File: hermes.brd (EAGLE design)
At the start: 22.9 x 35.1 mm, 36 parts

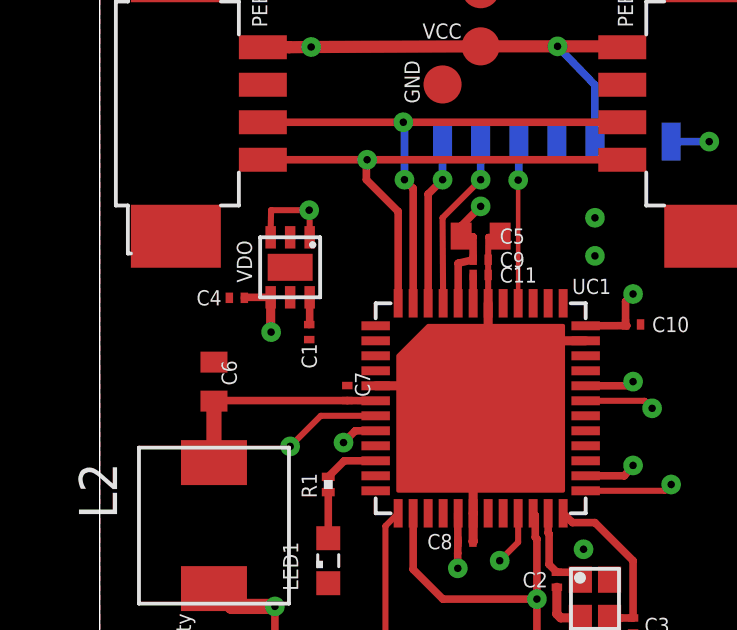
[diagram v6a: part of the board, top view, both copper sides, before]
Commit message: -Update component description in library -Generate new BOM and CAM files from new configuration -Delete outdated layout and cam documents
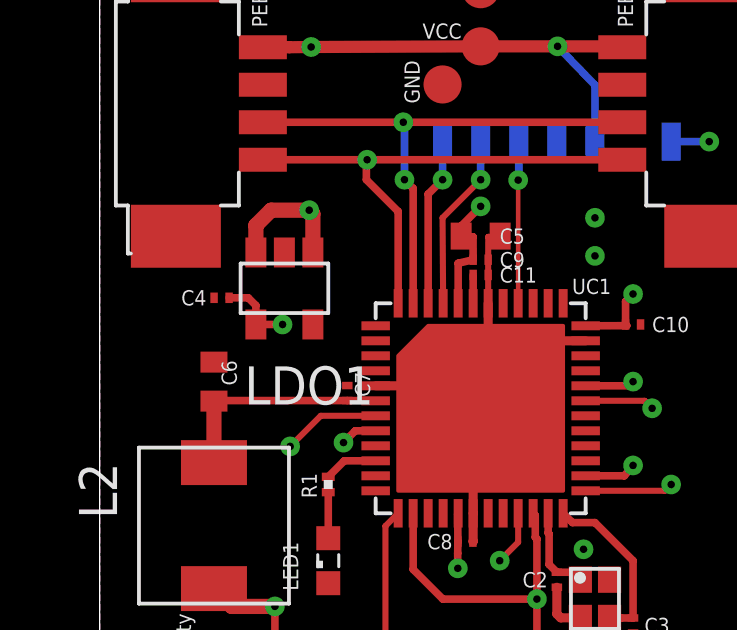
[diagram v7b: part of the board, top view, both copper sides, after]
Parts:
- removed C1: 470pF, rcl:C0201
- removed VDO: MIC5219-3.3BML, Hermes_lib:MLF-6
- added LDO1: MIC5231-3.3BM5, Hermes_lib:SOT-23-5
- moved C4 0.51 mm to (40.9, 32.9)
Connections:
- removed net N$2: C1.1, VDO.P$6
- net +3V3: now also LDO1.P$4; no longer VDO.P$4
- net GND: now also LDO1.P$2; no longer C1.2, VDO.P$2, VDO.P$7
- net VCC: now also LDO1.P$1, LDO1.P$3; no longer VDO.P$1, VDO.P$3
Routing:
- net VCC: track 24.2 -> 25.5 mm
- net N$2: track 0.92 -> 0.00 mm
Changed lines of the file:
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@@
 </autorouter>
 <elements>
-<element name="C1" library="rcl" library_urn="urn:adsk.eagle:library:334" package="C0201" package3d_urn="urn:adsk.eagle:package:23690/1" value="470pF" x="43.815" y="31.75" smashed="yes" rot="R270">
-<attribute name="NAME" x="43.561" y="31.369" size="0.508" layer="25" rot="R270"/>
-<attribute name="VALUE" x="41.91" y="32.385" size="0.508" layer="27" rot="R270"/>
-</element>
 <element name="C10" library="rcl" library_urn="urn:adsk.eagle:library:334" package="C0201" package3d_urn="urn:adsk.eagle:package:23690/1" value="100nF" x="54.61" y="32.004" smashed="yes">
 <attribute name="NAME" x="55.245" y="31.75" size="0.508" layer="25"/>
@@
 <attribute name="VALUE" x="52.705" y="22.606" size="0.508" layer="27" rot="R270"/>
 </element>
-<element name="C4" library="rcl" library_urn="urn:adsk.eagle:library:334" package="C0201" package3d_urn="urn:adsk.eagle:package:23690/1" value="2.2uF" x="41.402" y="32.893" smashed="yes" rot="R180">
-<attribute name="NAME" x="40.894" y="33.147" size="0.508" layer="25" rot="R180"/>
-<attribute name="VALUE" x="42.037" y="34.798" size="0.508" layer="27" rot="R180"/>
+<element name="C4" library="rcl" library_urn="urn:adsk.eagle:library:334" package="C0201" package3d_urn="urn:adsk.eagle:package:23690/1" value="2.2uF" x="40.894" y="32.893" smashed="yes" rot="R180">
+<attribute name="NAME" x="40.386" y="33.147" size="0.508" layer="25" rot="R180"/>
+<attribute name="VALUE" x="41.529" y="34.798" size="0.508" layer="27" rot="R180"/>
 </element>
 <element name="C5" library="rcl" library_urn="urn:adsk.eagle:library:334" package="C0402" package3d_urn="urn:adsk.eagle:package:23626/1" value="10uF" x="49.53" y="34.9504" smashed="yes">
@@
 <element name="PEER2" library="Hermes_lib" package="PICO-BLADE4" value="PICO-BLADE4" x="57.15" y="39.37" smashed="yes" rot="R90">
 <attribute name="NAME" x="54.61" y="41.91" size="0.508" layer="25" rot="R90"/>
-</element>
-<element name="VDO" library="Hermes_lib" package="MLF-6" value="MIC5219-3.3BML" x="43.18" y="33.909" smashed="yes" rot="R270">
-<attribute name="NAME" x="41.91" y="33.401" size="0.508" layer="25" rot="R90"/>
-<attribute name="VALUE" x="41.68" y="34.909" size="0.508" layer="27" rot="R270"/>
 </element>
 <element name="LED1" library="eagle-ltspice" library_urn="urn:adsk.eagle:library:217" package="LED_SML0603" package3d_urn="urn:adsk.eagle:package:13315/1" value="" x="44.45" y="24.13" smashed="yes" rot="R90">
@@
 </element>
 <element name="L2" library="Hermes_lib" package="L2215" value="10uH" x="40.64" y="25.4" rot="R270"/>
+<element name="LDO1" library="Hermes_lib" package="SOT-23-5" value="MIC5231-3.3BM5" x="42.926" y="33.147"/>
 </elements>
 <signals>
@@
 <contactref element="UC1" pad="P$36"/>
 <contactref element="C8" pad="1"/>
-<contactref element="VDO" pad="P$4"/>
 <contactref element="C4" pad="1"/>
 <contactref element="R4" pad="1"/>
@@
 <contactref element="R5" pad="2"/>
 <contactref element="SLAVE" pad="P$9"/>
-<wire x1="41.668" y1="32.909" x2="42.53" y2="32.909" width="0.254" layer="1"/>
-<wire x1="41.668" y1="32.909" x2="41.652" y2="32.893" width="0.254" layer="1"/>
 <polygon width="0.3048" layer="2">
 <vertex x="36.83" y="46.355"/>
@@
 <vertex x="59.69" y="46.355"/>
 </polygon>
-<wire x1="42.53" y1="32.909" x2="42.53" y2="31.765" width="0.3048" layer="1"/>
-<wire x1="42.53" y1="31.765" x2="42.545" y2="31.75" width="0.3048" layer="1"/>
-<via x="42.545" y="31.75" extent="1-16" drill="0.25"/>
 <wire x1="52.655" y1="16.743" x2="52.655" y2="18.873" width="0.3048" layer="1"/>
 <wire x1="52.655" y1="18.873" x2="52.705" y2="18.923" width="0.3048" layer="1"/>
@@
 <wire x1="42.672" y1="22.606" x2="41.234" y2="22.606" width="0.508" layer="1"/>
 <wire x1="41.234" y1="22.606" x2="40.64" y2="23.2" width="0.508" layer="1"/>
+<contactref element="LDO1" pad="P$4"/>
+<via x="42.926" y="32.004" extent="1-16" drill="0.25"/>
+<wire x1="41.144" y1="32.893" x2="41.783" y2="32.893" width="0.254" layer="1"/>
+<wire x1="41.783" y1="32.893" x2="42.037" y2="32.639" width="0.254" layer="1"/>
+<wire x1="42.037" y1="32.639" x2="42.037" y2="32.004" width="0.254" layer="1"/>
+<wire x1="42.037" y1="32.004" x2="42.926" y2="32.004" width="0.254" layer="1"/>
 </signal>
 <signal name="GND">
@@
 <contactref element="C8" pad="2"/>
 <contactref element="C4" pad="2"/>
-<contactref element="VDO" pad="P$2"/>
 <contactref element="LED1" pad="C"/>
 <contactref element="LED2" pad="C"/>
 <contactref element="C2" pad="2"/>
 <contactref element="C3" pad="2"/>
-<contactref element="C1" pad="2"/>
 <contactref element="XTAL" pad="GND@2"/>
 <contactref element="XTAL" pad="GND@1"/>
@@
 <vertex x="59.69" y="46.355"/>
 </polygon>
-<contactref element="VDO" pad="P$7"/>
 <wire x1="49.28" y1="28.96" x2="49.28" y2="25.71" width="0.3048" layer="1"/>
 <wire x1="49.53" y1="29.21" x2="49.28" y2="28.96" width="0.3048" layer="1"/>
@@
 <vertex x="59.69" y="11.303"/>
 </polygon>
+<contactref element="LDO1" pad="P$2"/>
 </signal>
 <signal name="VCC">
-<contactref element="VDO" pad="P$3"/>
-<contactref element="VDO" pad="P$1"/>
 <contactref element="PIN1" pad="P$1"/>
 <contactref element="VCC" pad="TP"/>
@@
 <via x="43.815" y="35.814" extent="1-16" drill="0.25"/>
 <via x="43.880634375" y="41.25324375" extent="1-16" drill="0.25"/>
-<wire x1="42.53" y1="34.909" x2="42.53" y2="35.164" width="0.2032" layer="1"/>
-<wire x1="42.53" y1="35.164" x2="42.545" y2="35.814" width="0.2032" layer="1"/>
-<wire x1="43.815" y1="35.814" x2="42.545" y2="35.814" width="0.2032" layer="1"/>
-<wire x1="43.83" y1="34.909" x2="43.83" y2="35.799" width="0.2032" layer="1"/>
 <wire x1="43.83" y1="35.799" x2="43.815" y2="35.814" width="0.2032" layer="1"/>
 <wire x1="43.815" y1="41.187609375" x2="43.880634375" y2="41.25324375" width="0.254" layer="2"/>
 <wire x1="43.815" y1="35.814" x2="43.815" y2="41.187609375" width="0.254" layer="2"/>
+<contactref element="LDO1" pad="P$3"/>
+<contactref element="LDO1" pad="P$1"/>
+<wire x1="43.815" y1="35.78955" x2="43.815" y2="35.814" width="0.508" layer="1"/>
+<wire x1="42.037" y1="34.404" x2="42.037" y2="35.306" width="0.508" layer="1"/>
+<wire x1="42.037" y1="35.306" x2="42.545" y2="35.814" width="0.508" layer="1"/>
+<wire x1="42.545" y1="35.814" x2="43.79055" y2="35.814" width="0.508" layer="1"/>
+<wire x1="43.79055" y1="35.814" x2="43.815" y2="35.78955" width="0.508" layer="1"/>
+<wire x1="43.937" y1="34.404" x2="43.937" y2="35.692" width="0.508" layer="1"/>
+<wire x1="43.937" y1="35.692" x2="43.83" y2="35.799" width="0.508" layer="1"/>
 </signal>
 <signal name="LED">
@@
 <via x="46.95126875" y="38.745" extent="1-16" drill="0.25"/>
 </signal>
-<signal name="N$2">
-<contactref element="VDO" pad="P$6"/>
-<contactref element="C1" pad="1"/>
-<wire x1="43.83" y1="32.909" x2="43.831" y2="32.016" width="0.254" layer="1"/>
-<wire x1="43.831" y1="32.016" x2="43.815" y2="32" width="0.254" layer="1"/>
-</signal>
 <signal name="N$3">
